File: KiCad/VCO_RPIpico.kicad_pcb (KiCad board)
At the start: 2 copper layers, 142 x 81 mm, 51 parts, among them J1 AudioJack2, J2 Power Jack 5V, SW1 LFO1/2, SW2 Select LFO WaveForm, SW3 Fire4, SW4 Fire3, SW5 Fire2, SW6 Fire1, SW7 Shift2/Save, SW8 Shift1 / Select Bank, U1 PT2399 Modul

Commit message: PCB Layout
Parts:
- removed D12: ZMDxx, Diode_SMD:D_MiniMELF
- removed U1: PT2399 Modul, PT2399_modul:PT2399_modul
- added C10: 100n, Capacitor_SMD:C_0805_2012Metric_Pad1.18x1.45mm_HandSolder, B.Cu at (132.4, 58.9)
- added C11: 560pF, Capacitor_SMD:C_0805_2012Metric_Pad1.18x1.45mm_HandSolder, B.Cu at (155.0, 81.7)
- added C12: 3,9nF, Capacitor_SMD:C_0805_2012Metric_Pad1.18x1.45mm_HandSolder, B.Cu at (163.9, 87.1)
- added C13: 82nF, Capacitor_SMD:C_0805_2012Metric_Pad1.18x1.45mm_HandSolder, B.Cu at (155.0, 71.4)
- added C14: 100n, Capacitor_SMD:C_0805_2012Metric_Pad1.18x1.45mm_HandSolder, B.Cu at (140.3, 67.8)
- added C15: 100n, Capacitor_SMD:C_0805_2012Metric_Pad1.18x1.45mm_HandSolder, B.Cu at (140.3, 65.3)
- added C16: 3,3nF, Capacitor_SMD:C_0805_2012Metric_Pad1.18x1.45mm_HandSolder, B.Cu at (163.7, 74.4)
- added C17: 4,7µ, Capacitor_Tantalum_SMD:CP_EIA-2012-12_Kemet-R_Pad1.30x1.05mm_HandSolder, B.Cu at (162.4, 89.4)
- added C18: 4,7µ, Capacitor_Tantalum_SMD:CP_EIA-2012-12_Kemet-R_Pad1.30x1.05mm_HandSolder, B.Cu at (169.0, 84.6)
- added C19: 100n, Capacitor_SMD:C_0805_2012Metric_Pad1.18x1.45mm_HandSolder, B.Cu at (163.7, 76.7)
- added C20: 560pF, Capacitor_SMD:C_0805_2012Metric_Pad1.18x1.45mm_HandSolder, B.Cu at (155.0, 76.4)
- added C21: 10µ, Capacitor_SMD:CP_Elec_4x5.7, B.Cu at (165.0, 80.5)
- added C22: 82nF, Capacitor_SMD:C_0805_2012Metric_Pad1.18x1.45mm_HandSolder, B.Cu at (155.0, 66.3)
- added C23: 10µ, Capacitor_SMD:CP_Elec_4x5.7, B.Cu at (170.8, 74.1)
- added C7: 100n, Capacitor_SMD:C_1206_3216Metric, B.Cu at (146.7, 86.3)
- added C8: 100µ, Capacitor_SMD:CP_Elec_6.3x5.8, B.Cu at (126.7, 77.3)
- added C9: 47µ, Capacitor_SMD:CP_Elec_6.3x5.3, B.Cu at (137.0, 77.3)
- added R19: 10k, Resistor_SMD:R_1206_3216Metric, B.Cu at (137.6, 70.3)
- added R20: 10k, Resistor_SMD:R_1206_3216Metric, B.Cu at (158.6, 84.6)
- added R21: 10k, Resistor_SMD:R_1206_3216Metric, B.Cu at (158.6, 82.0)
- added R22: 15k, Resistor_SMD:R_1206_3216Metric, B.Cu at (163.9, 84.6)
- added R23: 100k, Resistor_SMD:R_1206_3216Metric, B.Cu at (173.6, 80.6)
- added R24: 5,6k, Resistor_SMD:R_1206_3216Metric, B.Cu at (158.6, 79.5)
- added R25: 15k, Resistor_SMD:R_1206_3216Metric, B.Cu at (158.6, 76.9)
- added R26: 10k, Resistor_SMD:R_1206_3216Metric, B.Cu at (158.6, 74.4)
- added R27: 4,7k, Resistor_SMD:R_1206_3216Metric, B.Cu at (170.8, 80.6)
- added R28: 10k, Resistor_SMD:R_1206_3216Metric, B.Cu at (95.3, 59.7)
- added R29: 10k, Resistor_SMD:R_1206_3216Metric, B.Cu at (158.6, 71.9)
- added U2: PT2399, Package_DIP:DIP-16_W7.62mm_Socket_LongPads, B.Cu at (144.5, 83.0)
- added U3: L7805, Package_TO_SOT_SMD:TO-252-3_TabPin2, B.Cu at (128.3, 53.6)
- C1: footprint Capacitor_SMD:CP_Elec_8x10.5 -> Capacitor_SMD:CP_Elec_6.3x5.8
- C2, C3, C4, C5, C6: footprint Capacitor_SMD:C_1210_3225Metric -> Capacitor_SMD:C_1206_3216Metric
- D10: value LED WF_Tri -> LED_WF_Tri
- D11: value LED WF_Saw -> LED_WF_Saw
- D8: value LED WF_Squ -> LED_WF_Squ
- J2: value Power Jack 5V -> Power Jack
- R10, R11, R12, R16, R17, R18, R2, R3, R7, R8, R9: value 100 -> 680
- RV5: value 100k -> 50k
- moved C1 29.4 mm to (118.5, 60.8), turned to -90 degrees
- moved R1 18.5 mm to (102.8, 70.1), turned to -90 degrees
- moved R2 9.34 mm to (146.6, 88.8), turned to 180 degrees
- moved R3 7.76 mm to (130.9, 89.6), turned to 90 degrees
- moved R7 2.30 mm to (111.1, 84.1), turned to 180 degrees
- moved R8 2.30 mm to (117.2, 84.1), turned to 180 degrees
- moved R12 2.30 mm to (123.3, 84.1), turned to 180 degrees
- moved R17 1.09 mm to (149.8, 93.0)
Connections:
- A1 pad 33: GNDA -> GND
- C1 pad 1: +5C -> Net-(U3-IN)
- C2 pad 1: GNDA -> GND
- C3 pad 1: GNDA -> GND
- C4 pad 1: GNDA -> GND
- C6 pad 1: GNDA -> GND
- J2 pad 1: +5C -> Net-(U3-IN)
- R1 pad 1: Net-(U1-In+) -> /Wave_out
- R13 pad 3: GNDA -> GND
- R13 pad MP: GND -> (no net)
- R14 pad 3: GNDA -> GND
- R14 pad MP: GND -> (no net)
- R15 pad 3: GNDA -> GND
- R15 pad MP: GND -> (no net)
- RV4 pad 1: Net-(U1-Mix_D) -> GND
- RV4 pad 2: Net-(U1-Mix_G) -> GND
- RV4 pad MP: GND -> (no net)
- RV5 pad 1: Net-(RV5-Pad1) -> GND
- RV5 pad MP: GND -> (no net)
- RV6 pad MP: GND -> (no net)
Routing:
- net GND: track 34.8 -> 140.7 mm
- net GNDA: track 103.4 -> 0.00 mm
- net +5C: track 28.1 -> 130.6 mm
- net Net-(C21-Pad2): track 0.00 -> 97.9 mm, vias 0 -> 1
- net /Wave_out: track 0.00 -> 82.2 mm, vias 0 -> 2
- net Net-(C17-Pad2): track 0.00 -> 78.5 mm, vias 0 -> 2
- net Net-(U3-IN): track 0.00 -> 39.4 mm
- net Net-(J1-PadS): track 0.00 -> 30.6 mm
- net Net-(U2-LPF1-OUT): track 0.00 -> 21.8 mm
- net Net-(A1-GPIO5): track 0.00 -> 19.8 mm
- net Net-(R28-Pad1): track 0.00 -> 12.2 mm, vias 0 -> 1
- net Net-(A1-GPIO16): track 87.9 -> 76.3 mm
- net Net-(C12-Pad2): track 0.00 -> 10.1 mm
- net Net-(U2-LPF2-OUT): track 0.00 -> 7.97 mm
- net Net-(C16-Pad1): track 0.00 -> 7.66 mm
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- added copper zone on F.Cu, net GND

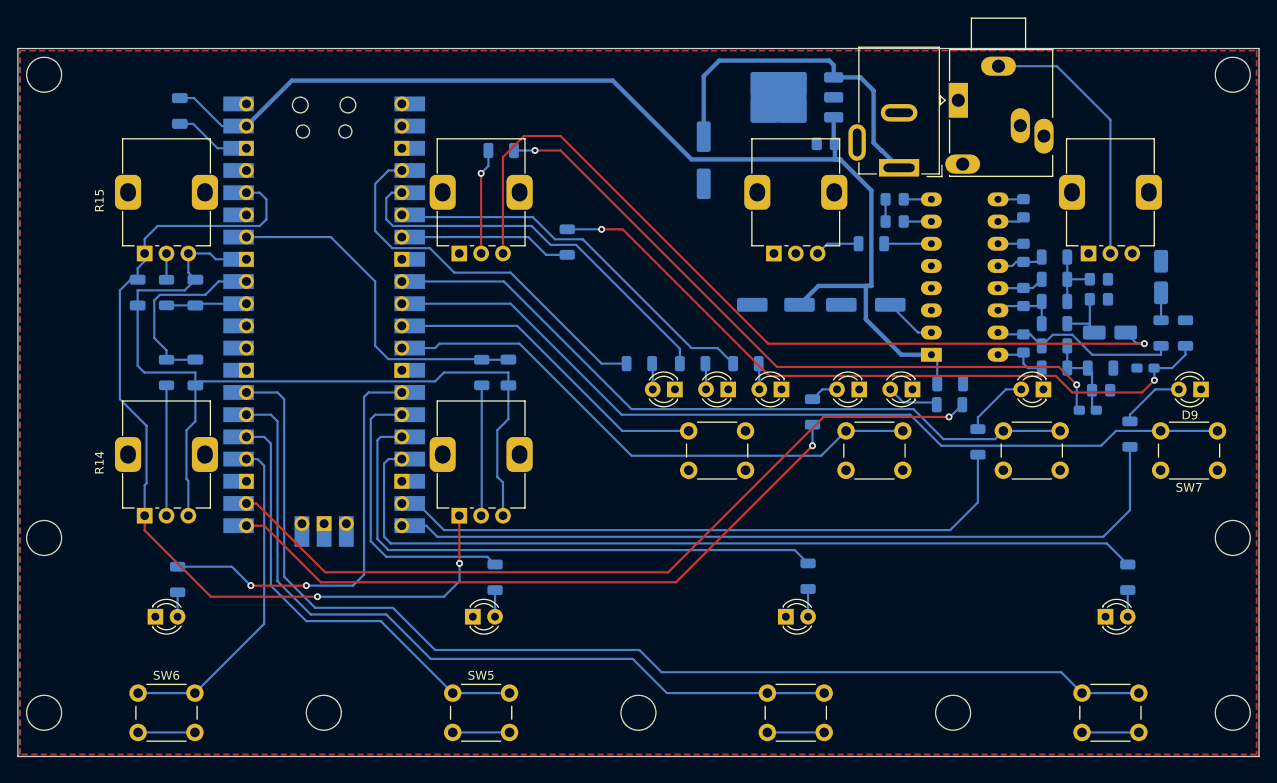
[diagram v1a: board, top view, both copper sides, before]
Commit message: PCB neue Taster
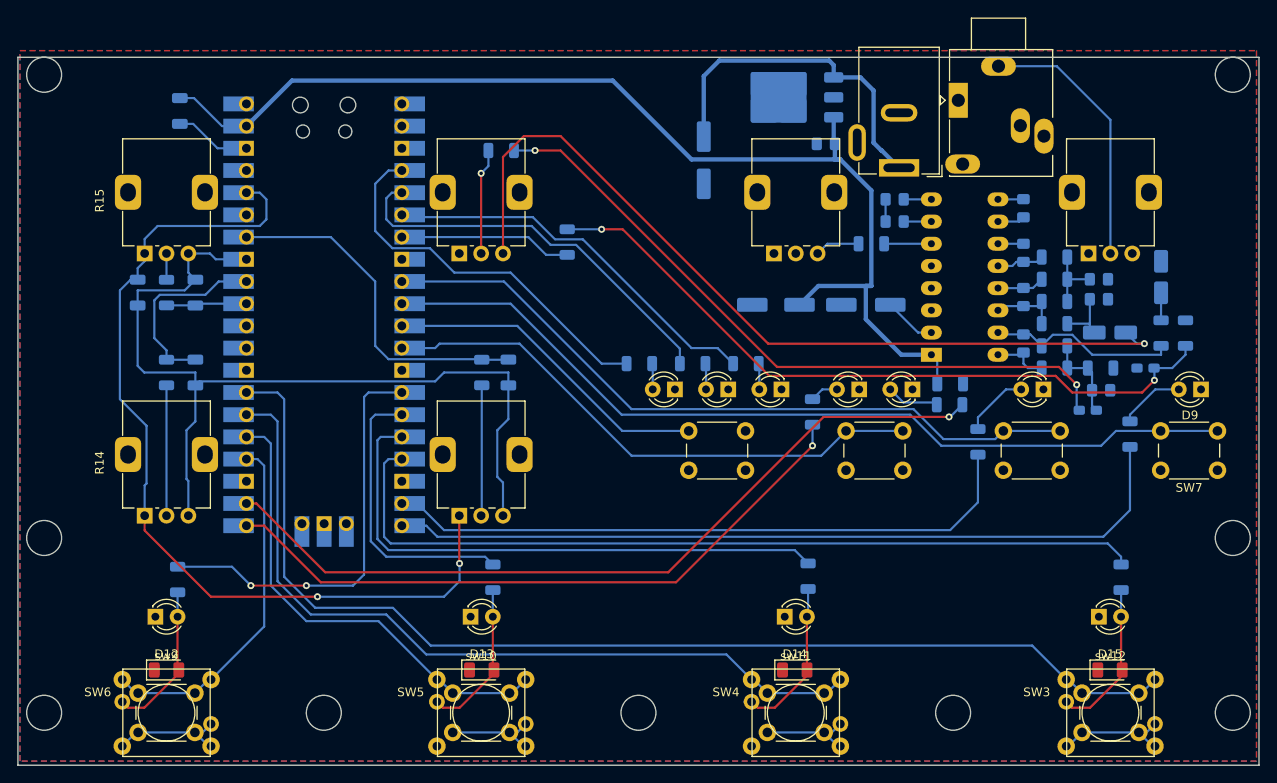
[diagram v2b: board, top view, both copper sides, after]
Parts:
- added D12: LED Fire1, LED_SMD:LED_1206_3216Metric, F.Cu at (57.0, 119.1)
- added D13: LED Fire2, LED_SMD:LED_1206_3216Metric, F.Cu at (93.1, 119.1)
- added D14: LED Fire3, LED_SMD:LED_1206_3216Metric, F.Cu at (128.9, 119.1)
- added D15: LED Fire4, LED_SMD:LED_1206_3216Metric, F.Cu at (165.0, 119.1)
- added sw10: sw_led_fire2, switches:Multimec Switch THT, F.Cu at (93.0, 124.0)
- added sw11: sw_led_fire3, switches:Multimec Switch THT, F.Cu at (129.0, 124.0)
- added sw12: sw_led_fire4, switches:Multimec Switch THT, F.Cu at (165.0, 124.0)
- added sw9: sw_led_fire1, switches:Multimec Switch THT, F.Cu at (57.0, 124.0)
- moved D7 0.76 mm to (163.7, 113.0)
- moved R16 0.76 mm to (166.2, 108.5)
- moved D5 0.25 mm to (91.8, 113.0)
- moved R10 0.25 mm to (94.3, 108.5)
- moved D6 0.13 mm to (127.7, 113.0)
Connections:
- net Net-(A1-GPIO18) renamed /sw_fire1
- net Net-(A1-GPIO19) renamed /sw_fire2
- net Net-(A1-GPIO20) renamed /sw_fire3
- net Net-(A1-GPIO21) renamed /sw_fire4
- net Net-(D4-A) renamed /led_fire1
- net Net-(D5-A) renamed /led_fire2
- net Net-(D6-A) renamed /led_fire3
- net Net-(D7-A) renamed /led_fire4
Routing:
- net GND: track 140.7 -> 164.7 mm
- net /led_fire4: track 3.05 -> 18.8 mm
- net /led_fire3: track 3.17 -> 18.9 mm
- net /led_fire2: track 3.05 -> 18.0 mm
- net /led_fire1: track 2.28 -> 17.2 mm
- net /sw_fire1: track 38.1 -> 40.8 mm
- net /sw_fire4: track 128.3 -> 130.8 mm
- net /sw_fire3: track 90.0 -> 92.5 mm
- net /sw_fire2: track 51.8 -> 54.3 mm
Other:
- outline, holes or cut-outs redrawn

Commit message: PCB fertig, Gerber Export
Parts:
- C19: value 100n -> 10n
- moved J2 28.5 mm to (168.8, 56.0)
- moved C1 7.53 mm to (119.2, 53.3)
- moved J1 6.83 mm to (144.1, 48.0)
- moved R29 2.37 mm to (157.9, 69.6), turned to 90 degrees
- moved R12 1.30 mm to (123.3, 82.8)
- moved R7 1.30 mm to (111.1, 82.8)
- moved R8 1.30 mm to (117.2, 82.8)
- moved C17 0.52 mm to (162.9, 89.4)
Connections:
- R13 pad MP: (no net) -> GND
- R14 pad MP: (no net) -> GND
- R15 pad MP: (no net) -> GND
- RV4 pad MP: (no net) -> GND
- RV5 pad MP: (no net) -> GND
- RV6 pad MP: (no net) -> GND
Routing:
- net GND: track 164.7 -> 145.4 mm
- net Net-(U3-IN): track 39.4 -> 58.0 mm
- net Net-(J1-PadS): track 30.6 -> 37.7 mm
- net Net-(A1-GPIO8): track 37.8 -> 44.3 mm
- net Net-(C16-Pad1): track 7.66 -> 12.3 mm
- net Net-(A1-GPIO28_ADC2): track 40.1 -> 35.8 mm
- net Net-(C23-Pad2): track 0.00 -> 3.67 mm
- net Net-(C18-Pad1): track 0.00 -> 2.70 mm
- net Net-(A1-GPIO3): track 45.9 -> 44.6 mm
- net Net-(D10-A): track 2.98 -> 4.28 mm
- net Net-(D11-A): track 2.98 -> 4.27 mm
- net Net-(D8-A): track 2.98 -> 4.26 mm
- net Net-(U2-OP2-OUT): track 5.43 -> 6.47 mm
- net Net-(A1-GPIO9): track 64.7 -> 64.0 mm
- net /led_fire4: track 18.8 -> 19.3 mm
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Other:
- board size 142 x 81 mm -> 142 x 88 mm

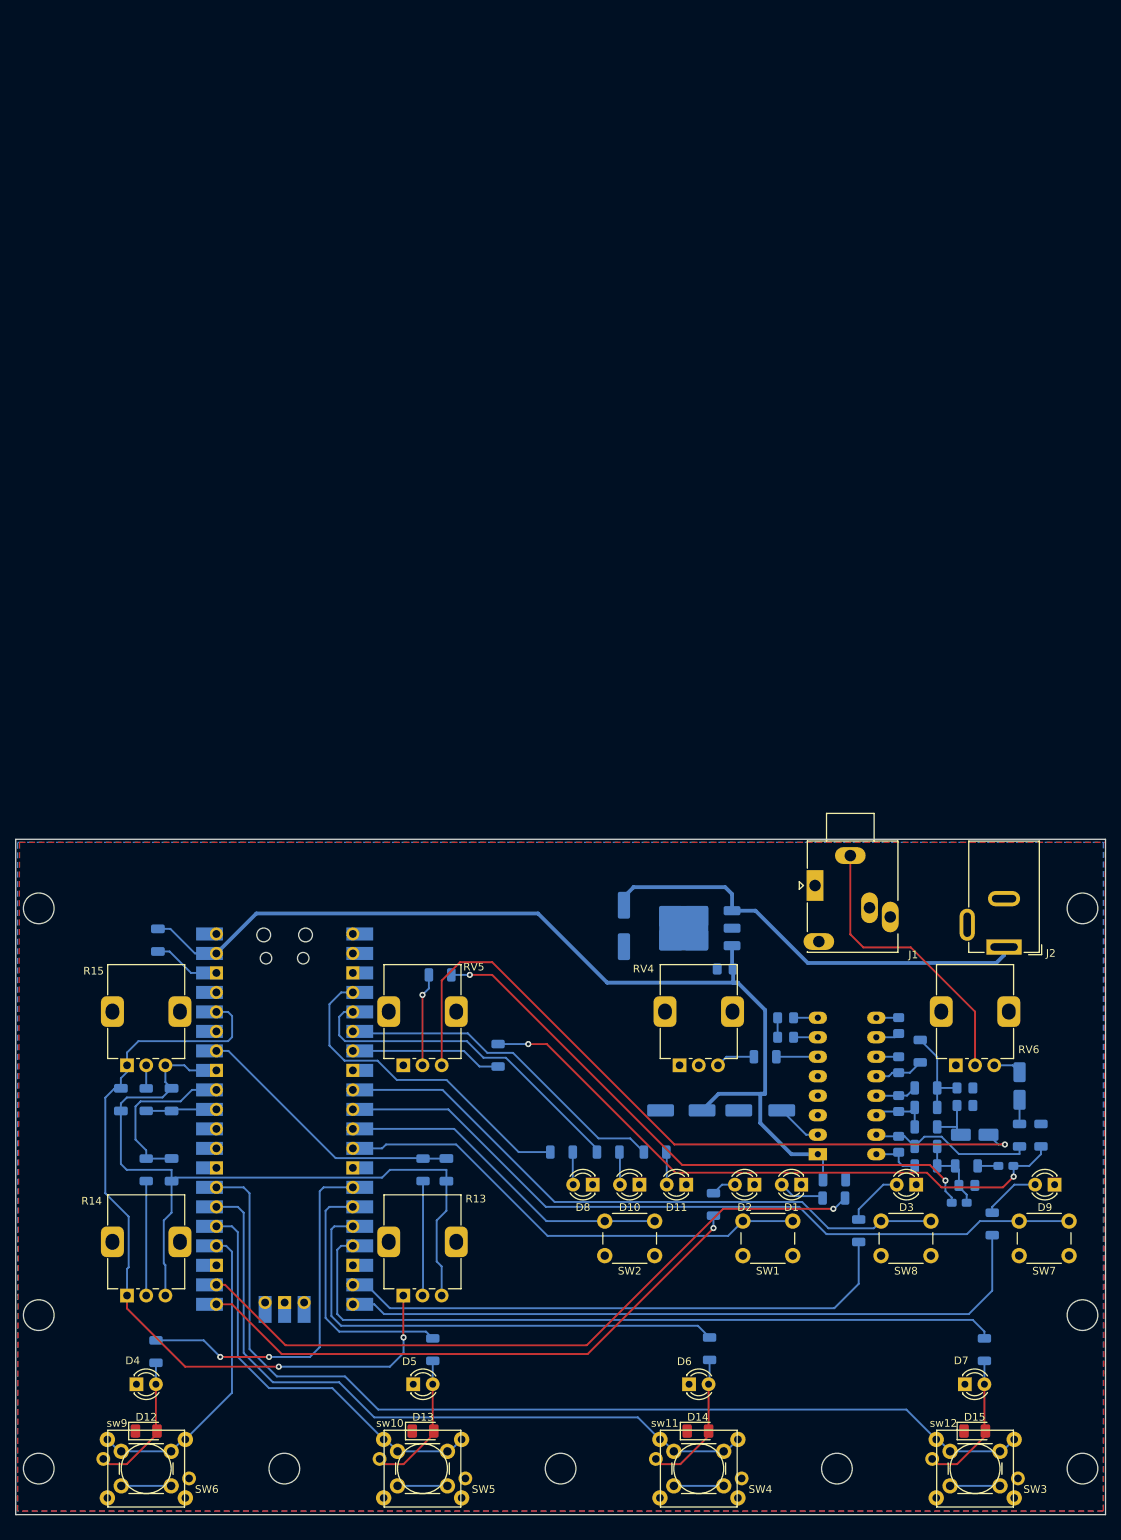
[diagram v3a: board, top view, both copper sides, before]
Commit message: zusätzliche LEDs unter die kleinen FIre-Button
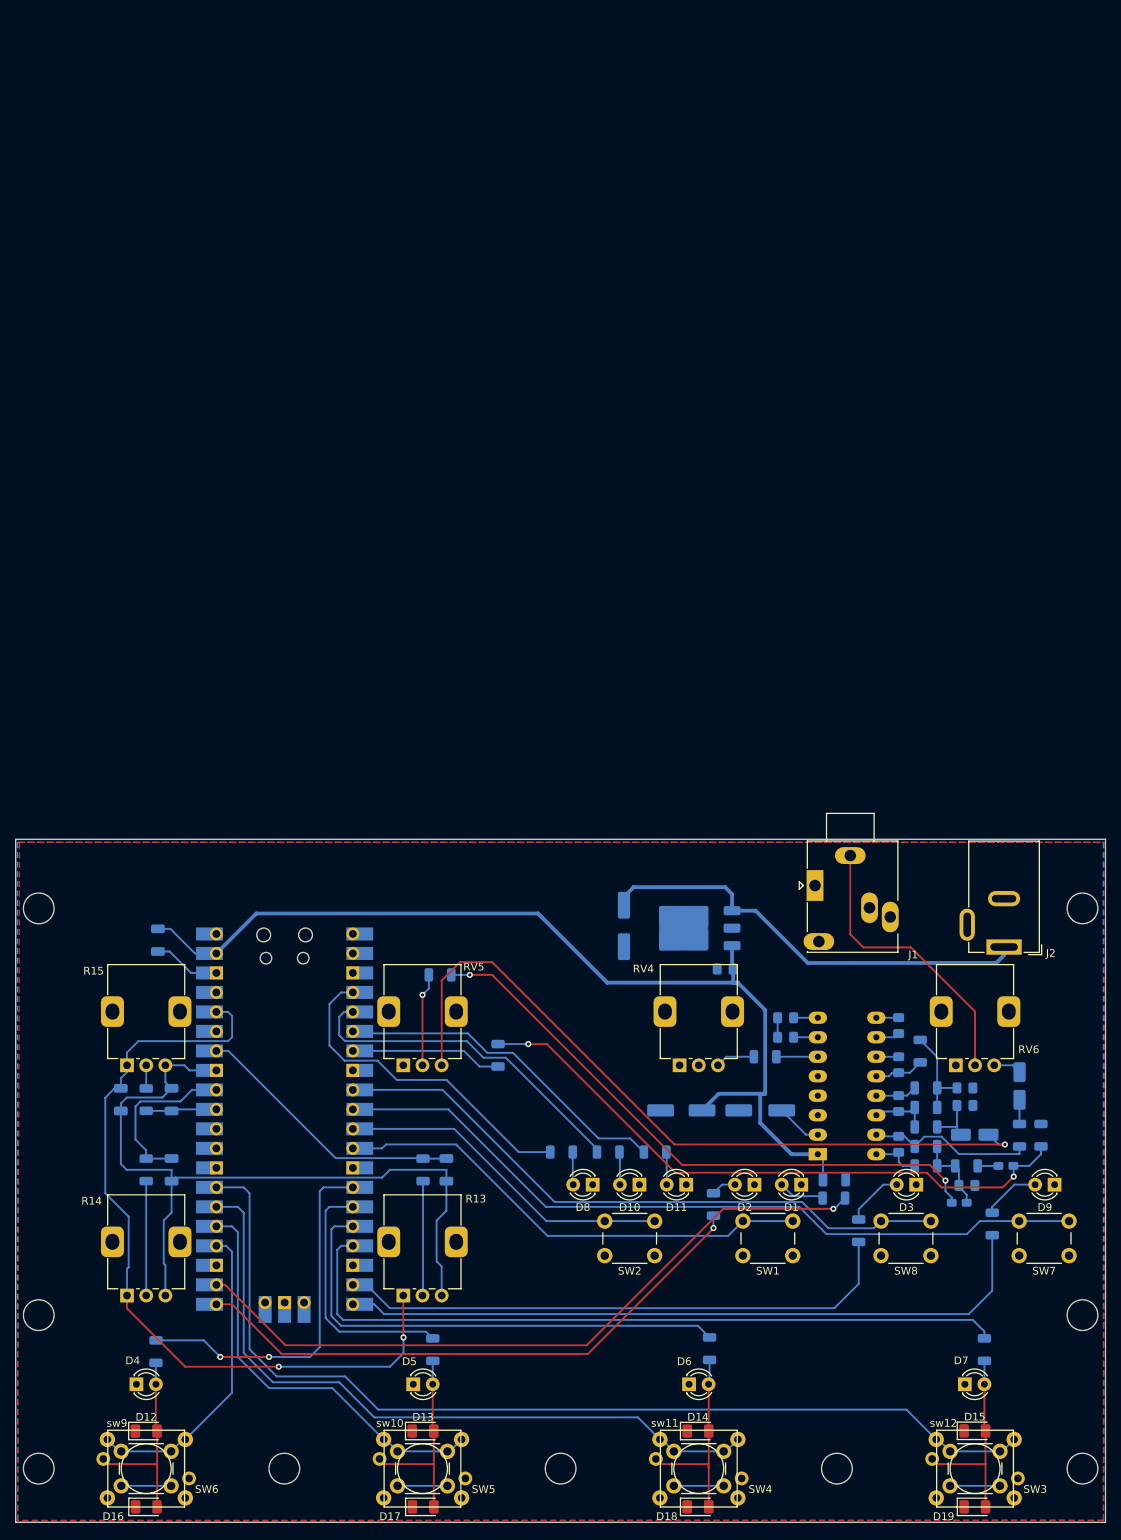
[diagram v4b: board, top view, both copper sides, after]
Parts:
- added D16: LED Fire1, LED_SMD:LED_1206_3216Metric, F.Cu at (57.0, 129.0)
- added D17: LED Fire2, LED_SMD:LED_1206_3216Metric, F.Cu at (93.1, 129.0)
- added D18: LED Fire3, LED_SMD:LED_1206_3216Metric, F.Cu at (128.9, 129.0)
- added D19: LED Fire4, LED_SMD:LED_1206_3216Metric, F.Cu at (165.0, 129.0)
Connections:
- R13 pad MP: GND -> (no net)
- R14 pad MP: GND -> (no net)
- R15 pad MP: GND -> (no net)
- RV4 pad MP: GND -> (no net)
- RV5 pad MP: GND -> (no net)
- RV6 pad MP: GND -> (no net)
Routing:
- net /led_fire1: track 17.7 -> 26.3 mm
- net /led_fire4: track 19.3 -> 27.7 mm
- net /led_fire3: track 19.5 -> 27.8 mm
- net /led_fire2: track 18.6 -> 26.8 mm
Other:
- board size 142 x 88 mm -> 142 x 89 mm
